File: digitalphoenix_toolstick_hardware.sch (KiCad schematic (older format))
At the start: 28 parts

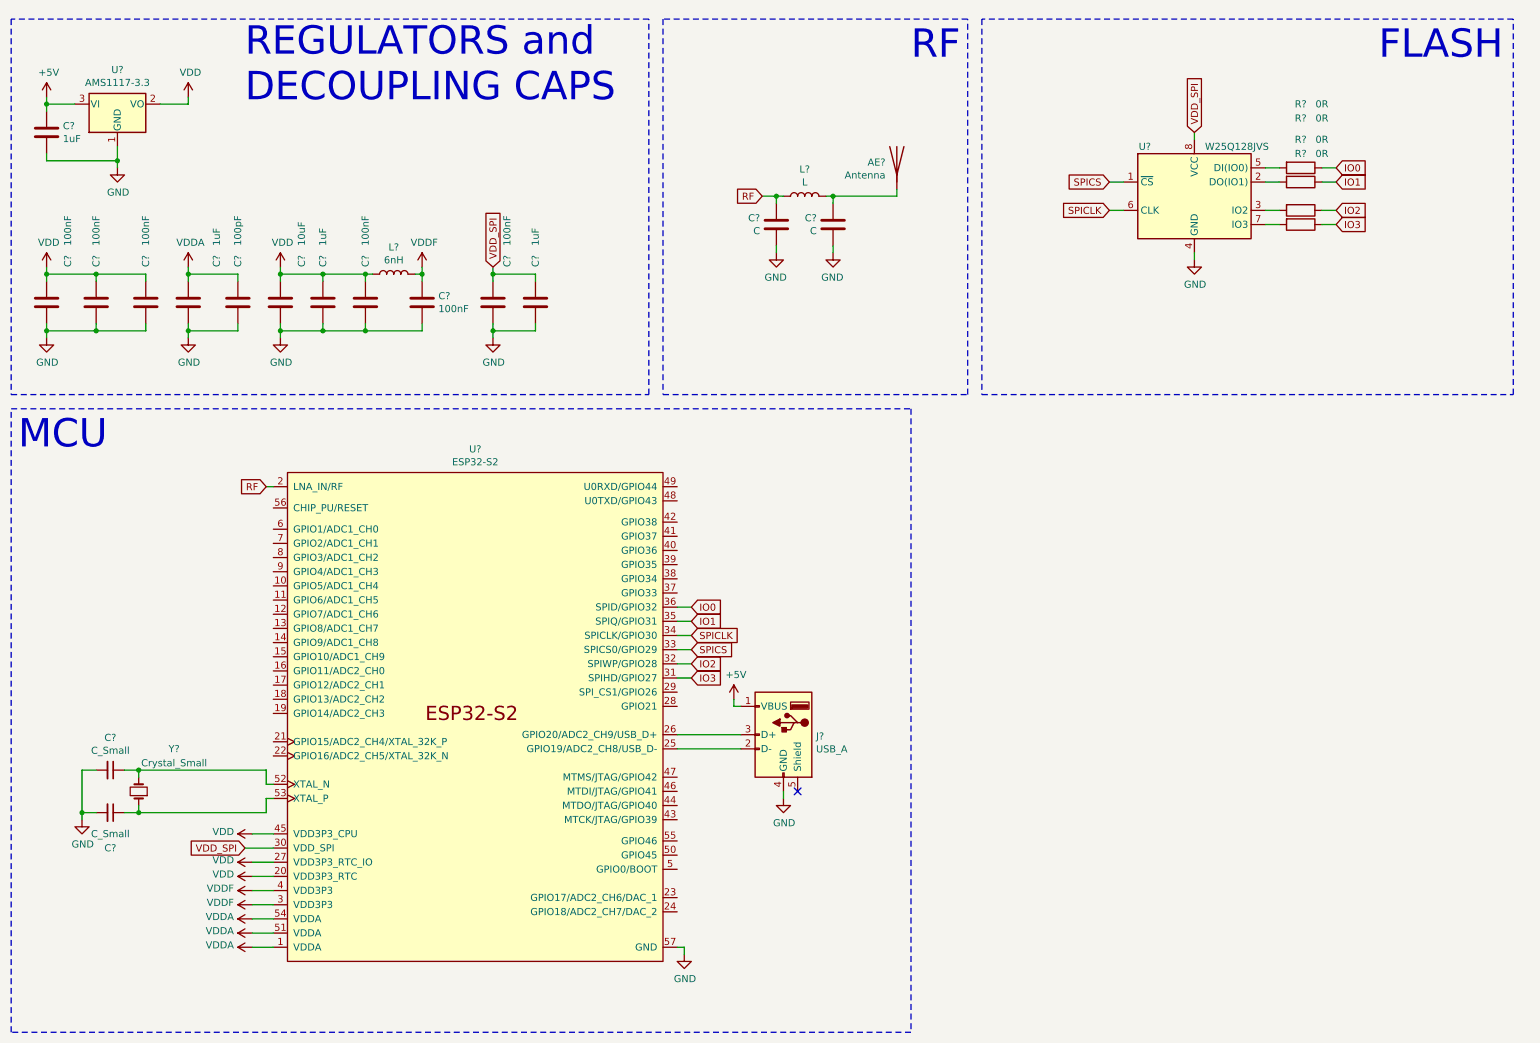
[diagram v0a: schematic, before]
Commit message: Working on V0.1 Schematic
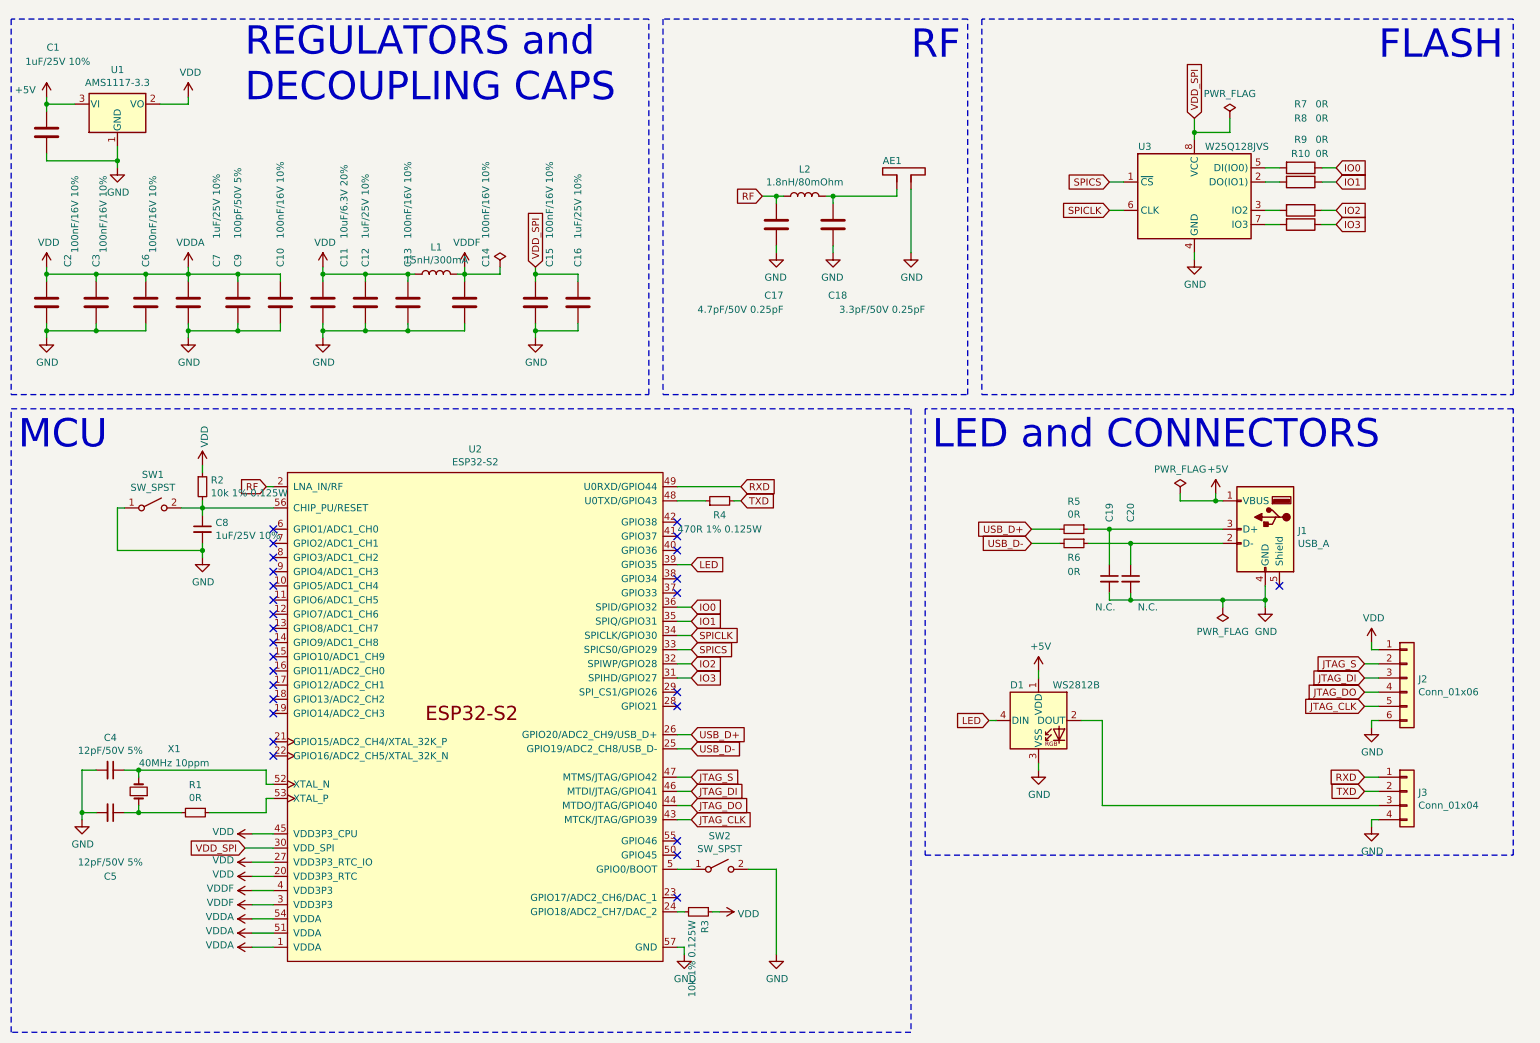
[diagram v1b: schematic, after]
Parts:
- removed AE?: Antenna, symbol Device:Antenna
- added AE1: 2.4GHz 50R Antenna, RF_Antenna:Texas_SWRA117D_2.4GHz_Left, symbol Device:Antenna_Dipole
- added C10: 100nF/16V 10%, Capacitor_SMD:C_0402_1005Metric, symbol Device:C
- added C19, C20: N.C., Capacitor_SMD:C_0402_1005Metric, symbol Device:C_Small
- added C8: 1uF/25V 10%, Capacitor_SMD:C_0402_1005Metric, symbol Device:C_Small
- added D1: WS2812B, LED_SMD:LED_WS2812B_PLCC4_5.0x5.0mm_P3.2mm, symbol LED:WS2812B
- added J2: Conn_01x06, Connector_PinSocket_2.54mm:PinSocket_1x06_P2.54mm_Vertical, symbol Connector_Generic:Conn_01x06
- added J3: Conn_01x04, Connector_PinSocket_2.54mm:PinSocket_1x04_P2.54mm_Vertical, symbol Connector_Generic:Conn_01x04
- added R1, R5, R6: 0R, Resistor_SMD:R_0402_1005Metric, symbol Device:R_Small
- added R2, R3: 10k 1% 0.125W, Resistor_SMD:R_0402_1005Metric, symbol Device:R_Small
- added R4: 470R 1% 0.125W, Resistor_SMD:R_0402_1005Metric, symbol Device:R_Small
- added SW1, SW2: SW_SPST, Button_Switch_SMD:SW_Push_SPST_NO_Alps_SKRK, symbol Switch:SW_SPST
- C1, C12, C16, C7: renamed from C?; value 1uF -> 1uF/25V 10%; footprint (none) -> Capacitor_SMD:C_0402_1005Metric; LCSC_Number (none) -> C52923
- C11: renamed from C?; value 10uF -> 10uF/6.3V 20%; footprint (none) -> Capacitor_SMD:C_0402_1005Metric; LCSC_Number (none) -> C15525
- C13, C14, C15, C2, C3, C6: renamed from C?; value 100nF -> 100nF/16V 10%; footprint (none) -> Capacitor_SMD:C_0402_1005Metric; LCSC_Number (none) -> C1525
- C17: renamed from C?; value C -> 4.7pF/50V 0.25pF; footprint (none) -> Capacitor_SMD:C_0402_1005Metric; LCSC_Number (none) -> C1569
- C18: renamed from C?; value C -> 3.3pF/50V 0.25pF; footprint (none) -> Capacitor_SMD:C_0402_1005Metric; LCSC_Number (none) -> C1565
- C4, C5: renamed from C?; value C_Small -> 12pF/50V 5%; footprint (none) -> Capacitor_SMD:C_0402_1005Metric; LCSC_Number (none) -> C1547
- C9: renamed from C?; value 100pF -> 100pF/50V 5%; footprint (none) -> Capacitor_SMD:C_0402_1005Metric; LCSC_Number (none) -> C1547
- J1: renamed from J?; footprint (none) -> SparkFun-Connectors:USB-A-PCB
- L1: renamed from L?; value 6nH -> 15nH/300mA; footprint (none) -> Inductor_SMD:L_0402_1005Metric; LCSC_Number (none) -> C27143
- L2: renamed from L?; value L -> 1.8nH/80mOhm; footprint (none) -> Inductor_SMD:L_0402_1005Metric; LCSC_Number (none) -> C77107
- R10, R7, R8, R9: renamed from R?; footprint (none) -> Resistor_SMD:R_0402_1005Metric; LCSC_Number (none) -> C17168
- U1: renamed from U?; LCSC_Number (none) -> C6186
- U2: renamed from U?; LCSC_Number (none) -> C529594
- U3: renamed from U?; LCSC_Number (none) -> C97521
- X1: renamed from Y?; value Crystal_Small -> 40MHz 10ppm; footprint (none) -> Crystal:Crystal_SMD_3225-4Pin_3.2x2.5mm; LCSC_Number (none) -> C90924
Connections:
- net VDDA is gone; now on net VDD: C7.1, C9.1, U2.1 (VDDA), U2.51 (VDDA), U2.54 (VDDA)
- net +5V: now also D1.1 (VDD)
- net GND: now also AE1.2, C10.2, C19.2, C20.2, C8.2, D1.3 (VSS), J2.6 (Pin_6), J3.4 (Pin_4), SW1.1 (A), SW2.2 (B)
- net VDD: now also C10.1, J2.1 (Pin_1), R2.1, R3.1
- net at U2.24 (GPIO18/ADC2_CH7/DAC_2): now also R3.2
- net at J1.2 (D-): now also C20.1, R6.1; no longer U2.25 (GPIO19/ADC2_CH8/USB_D-)
- net at J1.3 (D+): now also C19.1, R5.1; no longer U2.26 (GPIO20/ADC2_CH9/USB_D+)
- net LED: now reaches U2.39 (GPIO35)
- net LED: now also D1.4 (DIN)
- net JTAG_CLK: now reaches U2.43 (MTCK/JTAG/GPIO39)
- net JTAG_CLK: now also J2.5 (Pin_5)
- net JTAG_DO: now reaches U2.44 (MTDO/JTAG/GPIO40)
- net JTAG_DO: now also J2.4 (Pin_4)
- net JTAG_DI: now reaches U2.46 (MTDI/JTAG/GPIO41)
- net JTAG_DI: now also J2.3 (Pin_3)
- net JTAG_S: now reaches U2.47 (MTMS/JTAG/GPIO42)
- net JTAG_S: now also J2.2 (Pin_2)
- net at U2.48 (U0TXD/GPIO43): now also R4.1
- net RXD: now reaches U2.49 (U0RXD/GPIO44)
- net RXD: now also J3.1 (Pin_1)
- net at U2.5 (GPIO0/BOOT): now also SW2.1 (A)
- net at C5.1, X1.1: now also R1.2; no longer U2.53 (XTAL_P)
- net at U2.56 (CHIP_PU/RESET): now also C8.1, R2.2, SW1.2 (B)
- net at C18.1, L2.2: now also AE1.1
- new net: R1.1, U2.53 (XTAL_P)
- new net: D1.2 (DOUT), J3.3 (Pin_3)
- new net TXD: J3.2 (Pin_2), R4.2
- new net USB_D+: R5.2, U2.26 (GPIO20/ADC2_CH9/USB_D+)
- new net USB_D-: R6.2, U2.25 (GPIO19/ADC2_CH8/USB_D-)
- no-connect marks 1 -> 27
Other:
- note added: "LED and CONNECTORS"
- moved on the sheet: C11, C12, C13, C14, C15, C16, J1, L1

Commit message: Footprints and starting the PCB
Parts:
- J1: footprint SparkFun-Connectors:USB-A-PCB -> Wickerlib:CONN-USB-A-PCB-TRACES
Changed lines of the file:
@@
 F 0 "J1" H 9170 4139 50  0000 R CNN
 F 1 "USB_A" H 9170 4048 50  0000 R CNN
-F 2 "SparkFun-Connectors:USB-A-PCB" H 9550 4100 50  0001 C CNN
+F 2 "Wickerlib:CONN-USB-A-PCB-TRACES" H 9550 4100 50  0001 C CNN
 F 3 " ~" H 9550 4100 50  0001 C CNN
 	1    9400 4150

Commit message: More PCB work
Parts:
- removed X1: 40MHz 10ppm, Crystal:Crystal_SMD_3225-4Pin_3.2x2.5mm, symbol Device:Crystal_Small
- added X1: 40MHz 10ppm, Crystal:Crystal_SMD_3225-4Pin_3.2x2.5mm, symbol Device:Crystal_GND24_Small
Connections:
- net GND: now also X1.2, X1.4
- net at C4.1, U2.52 (XTAL_N): now also X1.1
- net at C5.1, R1.2: now also X1.3
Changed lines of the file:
@@
 	1450 5900 1450 5850
-$Comp
-L Device:Crystal_Small X1
-U 1 1 61AEB340
-P 1450 6000
-F 0 "X1" V 1750 5750 50  0000 C CNN
-F 1 "40MHz 10ppm" V 1650 5750 50  0000 C CNN
-F 2 "Crystal:Crystal_SMD_3225-4Pin_3.2x2.5mm" H 1450 6000 50  0001 C CNN
-F 3 "~" H 1450 6000 50  0001 C CNN
-F 4 "C90924" H 1450 6000 50  0001 C CNN "LCSC_Number"
-	1    1450 6000
-	0    -1   -1   0
-$EndComp
 $Comp
 L Memory_Flash:W25Q128JVS U3
@@
 U 1 1 61AFA7F2
 P 1850 6150
-F 0 "R1" V 1654 6150 50  0000 C CNN
-F 1 "0R" V 1745 6150 50  0000 C CNN
+F 0 "R1" V 1650 6200 50  0000 C CNN
+F 1 "0R" V 1750 6200 50  0000 C CNN
 F 2 "Resistor_SMD:R_0402_1005Metric" H 1850 6150 50  0001 C CNN
 F 3 "~" H 1850 6150 50  0001 C CNN
@@
 	-1   0    0    -1
 $EndComp
+$Comp
+L Device:Crystal_GND24_Small X1
+U 1 1 61B0F861
+P 1450 6000
+F 0 "X1" V 1700 5950 50  0000 L CNN
+F 1 "40MHz 10ppm" V 1800 5750 50  0000 L CNN
+F 2 "Crystal:Crystal_SMD_3225-4Pin_3.2x2.5mm" H 1450 6000 50  0001 C CNN
+F 3 "~" H 1450 6000 50  0001 C CNN
+F 4 "C90924" H 1450 6000 50  0001 C CNN "LCSC_Number"
+	1    1450 6000
+	0    1    1    0
+$EndComp
+$Comp
+L power:GND #PWR?
+U 1 1 61B18FAF
+P 1300 6000
+F 0 "#PWR?" H 1300 5750 50  0001 C CNN
+F 1 "GND" H 1305 5827 50  0000 C CNN
+F 2 "" H 1300 6000 50  0001 C CNN
+F 3 "" H 1300 6000 50  0001 C CNN
+	1    1300 6000
+	0    1    1    0
+$EndComp
+Wire Wire Line
+	1300 6000 1350 6000
+$Comp
+L power:GND #PWR?
+U 1 1 61B261D8
+P 1600 6000
+F 0 "#PWR?" H 1600 5750 50  0001 C CNN
+F 1 "GND" H 1605 5827 50  0000 C CNN
+F 2 "" H 1600 6000 50  0001 C CNN
+F 3 "" H 1600 6000 50  0001 C CNN
+	1    1600 6000
+	0    -1   -1   0
+$EndComp
+Wire Wire Line
+	1600 6000 1550 6000
 $EndSCHEMATC
